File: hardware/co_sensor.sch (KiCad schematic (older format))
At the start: 22 parts, among them P1 CONN28, P2 CONN28, P3 CONN6, U1 110-109, U2 AD8603, U3 AD8620

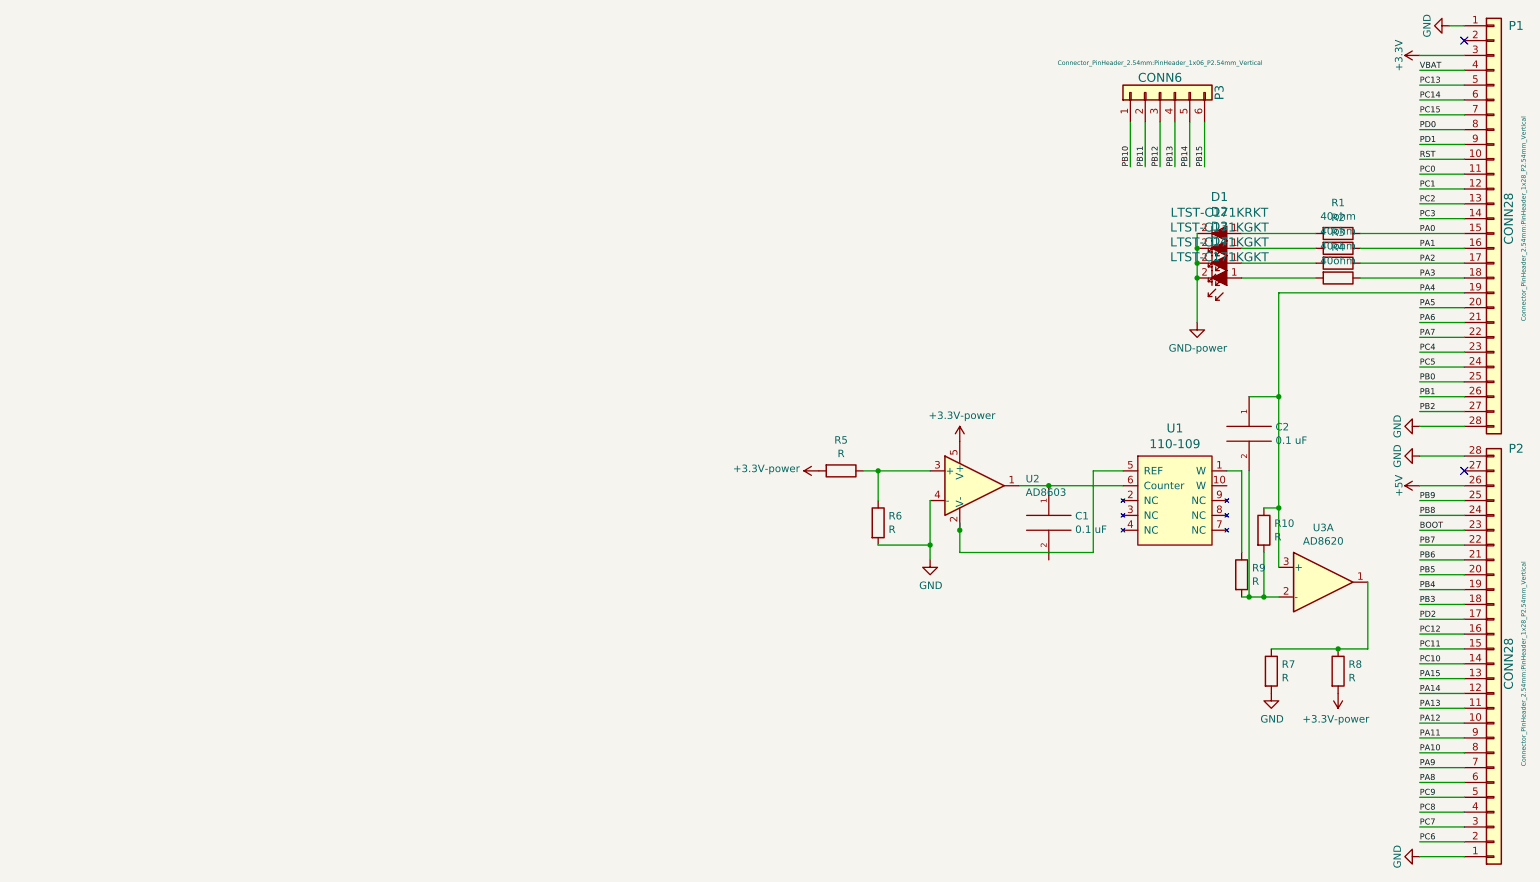
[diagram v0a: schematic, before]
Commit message: Completely refactors the board with a new sensor and processor. Adds a .gitignore
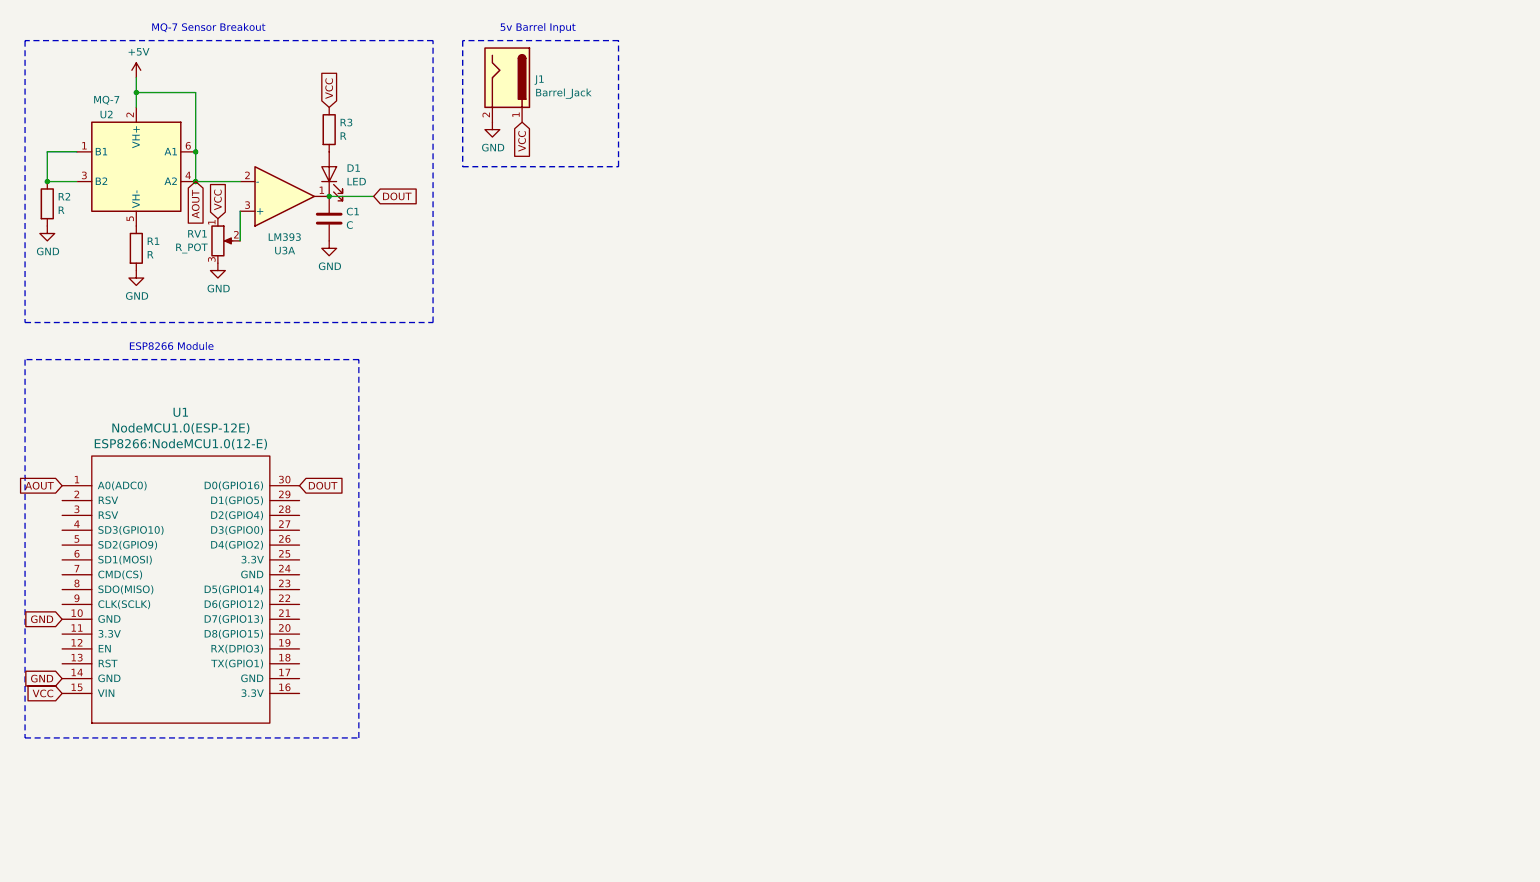
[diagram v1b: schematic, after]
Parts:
- removed C1, C2: 0.1 uF, smd_capacitor:C_1206_3216Metric, symbol pspice:C
- removed D1: LTST-C171KRKT, digikey-footprints:0805, symbol dk_LED-Indication-Discrete:LTST-C171KRKT
- removed D2, D3, D4: LTST-C171KGKT, digikey-footprints:0805, symbol dk_LED-Indication-Discrete:LTST-C171KGKT
- removed P1, P2: CONN28, Connector_PinHeader_2.54mm:PinHeader_1x28_P2.54mm_Vertical, symbol co_sensor-rescue:Conn_01x28-Connector_Generic
- removed P3: CONN6, Connector_PinHeader_2.54mm:PinHeader_1x06_P2.54mm_Vertical, symbol co_sensor-rescue:Conn_01x06-Connector_Generic
- removed R10, R5, R6, R7, R8, R9: R, smd_resistors:R_1206_3216Metric, symbol Device:R
- removed R4: 40ohm, SMD_Resistor_Footprints:R_1206_3216Metric, symbol Device:R
- removed U1: 110-109, digikey-footprints:Gas_Sensor_110-109, symbol dk_Gas-Sensors:110-109
- removed U2: AD8603, footprints:AD8603AUJZ-R2, symbol Amplifier_Operational:AD8603
- removed U3: AD8620, symbol Amplifier_Operational:AD8620
- added C1: C, Capacitor_SMD:C_0805_2012Metric, symbol Device:C
- added D1: LED, Diode_SMD:D_1206_3216Metric, symbol Device:LED
- added J1: Barrel_Jack, Connector_BarrelJack:BarrelJack_CUI_PJ-036AH-SMT_Horizontal, symbol Connector:Barrel_Jack
- added RV1: R_POT, Potentiometer_SMD:Potentiometer_ACP_CA9-VSMD_Vertical, symbol Device:R_POT
- added U1: NodeMCU1.0(ESP-12E), ESP8266:NodeMCU1.0(12-E), symbol ESP8266:NodeMCU1.0(ESP-12E)
- added U2: MQ-7, Sensor:MQ-6, symbol Sensor_Gas:MQ-6
- added U3: LM393, symbol Comparator:LM393
- R1, R2, R3: value 40ohm -> R; footprint SMD_Resistor_Footprints:R_1206_3216Metric -> Resistor_SMD:R_0805_2012Metric
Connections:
- net +5V: now also U1.1 (A0(ADC0)), U2.2 (VH+), U2.4 (A2), U2.6 (A1), U3.2 (-)
- net GND: now also R1.2, R2.2, C1.2, J1.2, RV1.3, U1.10 (GND), U1.14 (GND)
- net at R3.2: now also D1.2 (A)
- net PA0: no longer names the net of R1.1
- net PA0: now also U2.5 (VH-)
- net PA1: no longer names the net of R2.1
- net PA1: now also U2.1 (B1), U2.3 (B2)
- net PA2 renamed VCC
- net VCC: now also J1.1, RV1.1, U1.15 (VIN)
- new net: RV1.2, U3.3 (+)
- new net DOUT: C1.1, D1.1 (K), U1.30 (D0(GPIO16)), U3.1
- no-connect marks 2 -> 0
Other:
- note added: "5v Barrel Input"
- note added: "ESP8266 Module"
- note added: "MQ-7 Sensor Breakout"

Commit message: Updates with new LM393AR footprint and schematic item
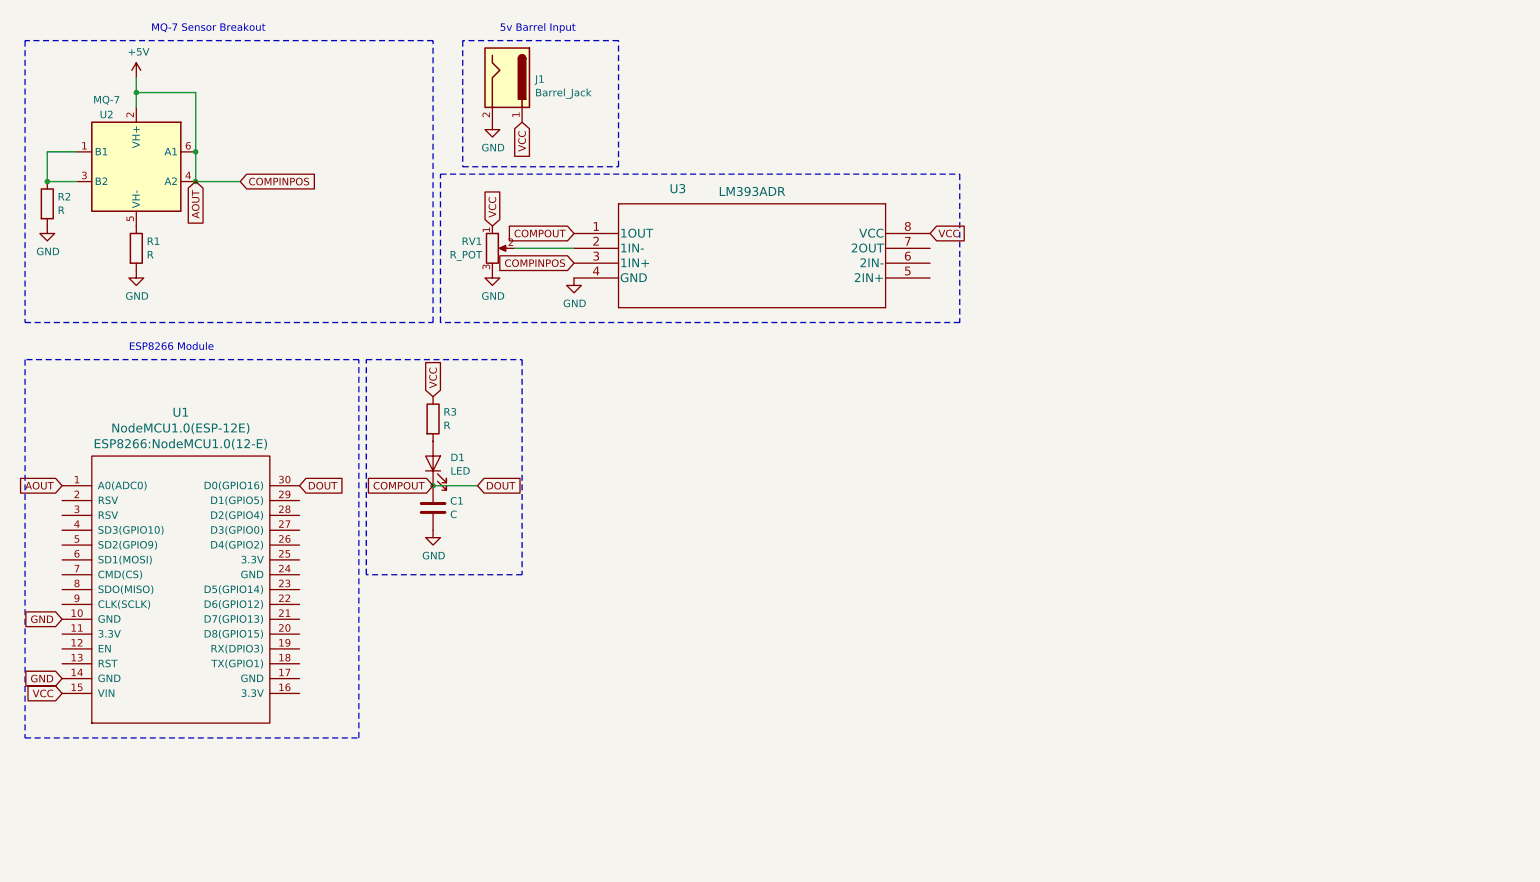
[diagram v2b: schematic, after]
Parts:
- removed U3: LM393, symbol Comparator:LM393
- added U3: LM393ADR, LM393AR:LM393ADR, symbol LM393AR:LM393ADR
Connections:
- net +5V: now also U3.3 (1IN+)
- net GND: now also U3.4 (GND)
- net VCC: now also U3.8 (VCC)
- net at RV1.2: now also U3.2 (1IN-)
- net DOUT renamed COMPOUT
- net COMPOUT: now also U3.1 (1OUT)
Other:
- moved on the sheet: C1, D1, R3, RV1
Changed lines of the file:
@@
 	1    0    0    -1
-$EndComp
-$Comp
-L Comparator:LM393 U3
-U 1 1 5EB3EC7D
-P 2550 1750
-F 0 "U3" H 2550 2117 50  0000 C CNN
-F 1 "LM393" H 2550 2026 50  0000 C CNN
-F 2 "" H 2550 1750 50  0001 C CNN
-F 3 "http://www.ti.com/lit/ds/symlink/lm393-n.pdf" H 2550 1750 50  0001 C CNN
-	1    2550 1750
-	1    0    0    1
 $EndComp
 Text GLabel 1950 1650 3    50   Input ~ 0
 AOUT
-$Comp
-L Device:R_POT RV1
-U 1 1 5EB43777
-P 2100 2050
-F 0 "RV1" H 2031 2096 50  0000 R CNN
-F 1 "R_POT" H 2031 2005 50  0000 R CNN
-F 2 "Potentiometer_SMD:Potentiometer_ACP_CA9-VSMD_Vertical" H 2100 2050 50  0001 C CNN
-F 3 "~" H 2100 2050 50  0001 C CNN
-	1    2100 2050
-	1    0    0    -1
-$EndComp
-$Comp
-L power:GND #PWR0105
-U 1 1 5EB4612A
-P 2100 2200
-F 0 "#PWR0105" H 2100 1950 50  0001 C CNN
-F 1 "GND" H 2105 2027 50  0000 C CNN
-F 2 "" H 2100 2200 50  0001 C CNN
-F 3 "" H 2100 2200 50  0001 C CNN
-	1    2100 2200
-	1    0    0    -1
-$EndComp
-Wire Wire Line
-	2250 1850 2250 2050
-Text GLabel 3150 1750 2    50   Input ~ 0
+Text GLabel 3850 3700 2    50   Input ~ 0
 DOUT
 $Comp
 L Device:LED D1
 U 1 1 5EB4CE34
-P 2850 1600
-F 0 "D1" V 2889 1483 50  0000 R CNN
-F 1 "LED" V 2798 1483 50  0000 R CNN
-F 2 "Diode_SMD:D_1206_3216Metric" H 2850 1600 50  0001 C CNN
-F 3 "~" H 2850 1600 50  0001 C CNN
-	1    2850 1600
+P 3550 3550
+F 0 "D1" V 3589 3433 50  0000 R CNN
+F 1 "LED" V 3498 3433 50  0000 R CNN
+F 2 "Diode_SMD:D_1206_3216Metric" H 3550 3550 50  0001 C CNN
+F 3 "~" H 3550 3550 50  0001 C CNN
+	1    3550 3550
 	0    -1   -1   0
 $EndComp
-Connection ~ 2850 1750
+Connection ~ 3550 3700
 Wire Wire Line
-	2850 1750 3150 1750
+	3550 3700 3850 3700
 $Comp
 L Device:R R3
 U 1 1 5EB4E0BD
-P 2850 1300
-F 0 "R3" H 2920 1346 50  0000 L CNN
-F 1 "R" H 2920 1255 50  0000 L CNN
-F 2 "Resistor_SMD:R_0805_2012Metric" V 2780 1300 50  0001 C CNN
-F 3 "~" H 2850 1300 50  0001 C CNN
-	1    2850 1300
+P 3550 3250
+F 0 "R3" H 3620 3296 50  0000 L CNN
+F 1 "R" H 3620 3205 50  0000 L CNN
+F 2 "Resistor_SMD:R_0805_2012Metric" V 3480 3250 50  0001 C CNN
+F 3 "~" H 3550 3250 50  0001 C CNN
+	1    3550 3250
 	1    0    0    -1
 $EndComp
@@
 L Device:C C1
 U 1 1 5EB4F120
-P 2850 1900
-F 0 "C1" H 2965 1946 50  0000 L CNN
-F 1 "C" H 2965 1855 50  0000 L CNN
-F 2 "Capacitor_SMD:C_0805_2012Metric" H 2888 1750 50  0001 C CNN
-F 3 "~" H 2850 1900 50  0001 C CNN
-	1    2850 1900
+P 3550 3850
+F 0 "C1" H 3665 3896 50  0000 L CNN
+F 1 "C" H 3665 3805 50  0000 L CNN
+F 2 "Capacitor_SMD:C_0805_2012Metric" H 3588 3700 50  0001 C CNN
+F 3 "~" H 3550 3850 50  0001 C CNN
+	1    3550 3850
 	1    0    0    -1
 $EndComp
@@
 L power:GND #PWR0107
 U 1 1 5EB4F930
-P 2850 2050
-F 0 "#PWR0107" H 2850 1800 50  0001 C CNN
-F 1 "GND" H 2855 1877 50  0000 C CNN
-F 2 "" H 2850 2050 50  0001 C CNN
-F 3 "" H 2850 2050 50  0001 C CNN
-	1    2850 2050
+P 3550 4000
+F 0 "#PWR0107" H 3550 3750 50  0001 C CNN
+F 1 "GND" H 3555 3827 50  0000 C CNN
+F 2 "" H 3550 4000 50  0001 C CNN
+F 3 "" H 3550 4000 50  0001 C CNN
+	1    3550 4000
 	1    0    0    -1
 $EndComp
@@
 Text GLabel 4150 1250 3    50   Input ~ 0
 VCC
-Text GLabel 2850 1150 1    50   Input ~ 0
-VCC
-Text GLabel 2100 1900 1    50   Input ~ 0
+Text GLabel 3550 3100 1    50   Input ~ 0
 VCC
 Text GLabel 1050 3700 0    50   Input ~ 0
@@
 Text Notes 1500 2800 0    50   ~ 0
 ESP8266 Module
+$Comp
+L LM393AR:LM393ADR U3
+U 1 1 5EB2D101
+P 4500 2000
+F 0 "U3" H 5200 2300 60  0000 C CNN
+F 1 "LM393ADR" H 5700 2281 60  0000 C CNN
+F 2 "LM393AR:LM393ADR" H 5700 2240 60  0001 C CNN
+F 3 "" H 4500 2000 60  0000 C CNN
+	1    4500 2000
+	1    0    0    -1
+$EndComp
+Text GLabel 3950 1950 1    50   Input ~ 0
+VCC
+$Comp
+L power:GND #PWR0105
+U 1 1 5EB4612A
+P 3950 2250
+F 0 "#PWR0105" H 3950 2000 50  0001 C CNN
+F 1 "GND" H 3955 2077 50  0000 C CNN
+F 2 "" H 3950 2250 50  0001 C CNN
+F 3 "" H 3950 2250 50  0001 C CNN
+	1    3950 2250
+	1    0    0    -1
+$EndComp
+$Comp
+L Device:R_POT RV1
+U 1 1 5EB43777
+P 3950 2100
+F 0 "RV1" H 3881 2146 50  0000 R CNN
+F 1 "R_POT" H 3881 2055 50  0000 R CNN
+F 2 "Potentiometer_SMD:Potentiometer_ACP_CA9-VSMD_Vertical" H 3950 2100 50  0001 C CNN
+F 3 "~" H 3950 2100 50  0001 C CNN
+	1    3950 2100
+	1    0    0    -1
+$EndComp
+Wire Wire Line
+	4100 2100 4500 2100
+Text GLabel 4500 2200 0    50   Input ~ 0
+COMPINPOS
+Text GLabel 4500 2000 0    50   Input ~ 0
+COMPOUT
+Text GLabel 6900 2000 2    50   Input ~ 0
+VCC
+$Comp
+L power:GND #PWR0104
+U 1 1 5EB4E5CC
+P 4500 2300
+F 0 "#PWR0104" H 4500 2050 50  0001 C CNN
+F 1 "GND" H 4505 2127 50  0000 C CNN
+F 2 "" H 4500 2300 50  0001 C CNN
+F 3 "" H 4500 2300 50  0001 C CNN
+	1    4500 2300
+	1    0    0    -1
+$EndComp
+Text GLabel 2250 1650 2    50   Input ~ 0
+COMPINPOS
+Text GLabel 3550 3700 0    50   Input ~ 0
+COMPOUT
+Wire Notes Line
+	3600 2600 3600 1600
+Wire Notes Line
+	3600 1600 7100 1600
+Wire Notes Line
+	7100 1600 7100 2600
+Wire Notes Line
+	7100 2600 3600 2600
+Wire Notes Line
+	3100 2850 4150 2850
+Wire Notes Line
+	4150 2850 4150 4300
+Wire Notes Line
+	4150 4300 3100 4300
+Wire Notes Line
+	3100 4300 3100 2850
 $EndSCHEMATC

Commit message: Adds gerber file and updates schematic to include hardware in BOM
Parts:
- removed J1: Barrel_Jack, Connector_BarrelJack:BarrelJack_CUI_PJ-036AH-SMT_Horizontal, symbol Connector:Barrel_Jack
- added J1: PJ1-022-SMT-TR, CUI_PJ1-022-SMT-TR, symbol PJ1-022-SMT:PJ1-022-SMT-TR
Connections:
- net GND: now also J1.2
- net VCC: now also J1.1
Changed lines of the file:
@@
 MQ-7 Sensor Breakout
-$Comp
-L Connector:Barrel_Jack J1
-U 1 1 5EB62775
-P 4050 950
-F 0 "J1" V 4061 1138 50  0000 L CNN
-F 1 "Barrel_Jack" V 4152 1138 50  0000 L CNN
-F 2 "Connector_BarrelJack:BarrelJack_CUI_PJ-036AH-SMT_Horizontal" H 4100 910 50  0001 C CNN
-F 3 "~" H 4100 910 50  0001 C CNN
-	1    4050 950
-	0    1    1    0
-$EndComp
 $Comp
 L power:GND #PWR0109
 U 1 1 5EB63CD1
-P 3950 1250
-F 0 "#PWR0109" H 3950 1000 50  0001 C CNN
-F 1 "GND" H 3955 1077 50  0000 C CNN
-F 2 "" H 3950 1250 50  0001 C CNN
-F 3 "" H 3950 1250 50  0001 C CNN
-	1    3950 1250
-	1    0    0    -1
+P 4400 1250
+F 0 "#PWR0109" H 4400 1000 50  0001 C CNN
+F 1 "GND" H 4405 1077 50  0000 C CNN
+F 2 "" H 4400 1250 50  0001 C CNN
+F 3 "" H 4400 1250 50  0001 C CNN
+	1    4400 1250
+	0    -1   -1   0
 $EndComp
 Wire Notes Line
@@
 Text Notes 4000 650  0    50   ~ 0
 5v Barrel Input
-Text GLabel 4150 1250 3    50   Input ~ 0
+Text GLabel 4400 1050 2    50   Input ~ 0
 VCC
 Text GLabel 3550 3100 1    50   Input ~ 0
@@
 Wire Notes Line
 	3100 4300 3100 2850
+$Comp
+L PJ1-022-SMT:PJ1-022-SMT-TR J1
+U 1 1 5EB6AA59
+P 4200 1150
+F 0 "J1" H 4195 1490 50  0000 C CNN
+F 1 "PJ1-022-SMT-TR" H 4195 1399 50  0000 C CNN
+F 2 "CUI_PJ1-022-SMT-TR" H 4200 1150 50  0001 L BNN
+F 3 "CUI INC" H 4200 1150 50  0001 L BNN
+F 4 "1.05" H 4200 1150 50  0001 L BNN "Field4"
+F 5 "Manufacturer recommendations" H 4200 1150 50  0001 L BNN "Field5"
+	1    4200 1150
+	1    0    0    -1
+$EndComp
 $EndSCHEMATC
